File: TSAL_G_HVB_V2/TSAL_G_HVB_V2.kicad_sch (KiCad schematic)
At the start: 44 parts, among them J1 Conn_01x03_Pin, J2 Conn_01x02_Pin, J3 Conn_01x02_Pin, J4 Conn_01x02_Pin, Q1 2N7002, Q2 MMBT3904, Q3 PMOS, U1 uA7805, U2 74HC86, U3 74AHC04, U4 74LS09, U5 NE555D

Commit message: TSAL GREEN SYSTEM V2 READY TO FAB
SCH&PCB updated for both HVB V2 and ACCUM V2

PCB is 9 draw at work btw
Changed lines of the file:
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@@
+		)
+	)
+	(global_label "SCS_SIGN_IN"
+		(shape input)
+		(at 45.466 152.908 180)
+		(fields_autoplaced yes)
+		(effects
+			(font
+				(size 1.27 1.27)
+			)
+			(justify right)
+		)
+		(property "Intersheetrefs" "${INTERSHEET_REFS}"
+			(at 30.5065 152.908 0)
+			(hide yes)
+			(show_name no)
+			(do_not_autoplace no)
+			(effects
+				(font
+					(size 1.27 1.27)
+				)
+				(justify right)
+			)
 		)
 	)
@@
 	(global_label "RELAY_AUX_STATE"
 		(shape input)
+		(at 50.038 157.734 180)
+		(fields_autoplaced yes)
+		(effects
+			(font
+				(size 1.27 1.27)
+			)
+			(justify right)
+		)
+		(property "Intersheetrefs" "${INTERSHEET_REFS}"
+			(at 30.4824 157.734 0)
+			(hide yes)
+			(show_name no)
+			(do_not_autoplace no)
+			(effects
+				(font
+					(size 1.27 1.27)
+				)
+				(justify right)
+			)
+		)
+	)
+	(global_label "HV_SIGN_IN"
+		(shape input)
+		(at 44.45 148.336 180)
+		(fields_autoplaced yes)
+		(effects
+			(font
+				(size 1.27 1.27)
+			)
+			(justify right)
+		)
+		(property "Intersheetrefs" "${INTERSHEET_REFS}"
+			(at 30.7604 148.336 0)
+			(hide yes)
+			(show_name no)
+			(do_not_autoplace no)
+			(effects
+				(font
+					(size 1.27 1.27)
+				)
+				(justify right)
+			)
+		)
+	)
+	(global_label "RELAY_AUX_STATE"
+		(shape input)
 		(at 32.258 32.512 0)
 		(fields_autoplaced yes)
@@
 			(hide yes)
 			(show_name no)
+			(do_not_autoplace no)
+			(effects
+				(font
+					(size 1.27 1.27)
+				)
+				(justify right)
+			)
+		)
+	)
+	(global_label "RELAY_INTENDED_STATE"
+		(shape input)
+		(at 55.626 163.322 180)
+		(fields_autoplaced yes)
+		(effects
+			(font
+				(size 1.27 1.27)
+			)
+			(justify right)
+		)
+		(property "Intersheetrefs" "${INTERSHEET_REFS}"
+			(at 30.6276 163.322 0)
+			(hide yes)
+			(show_name no)

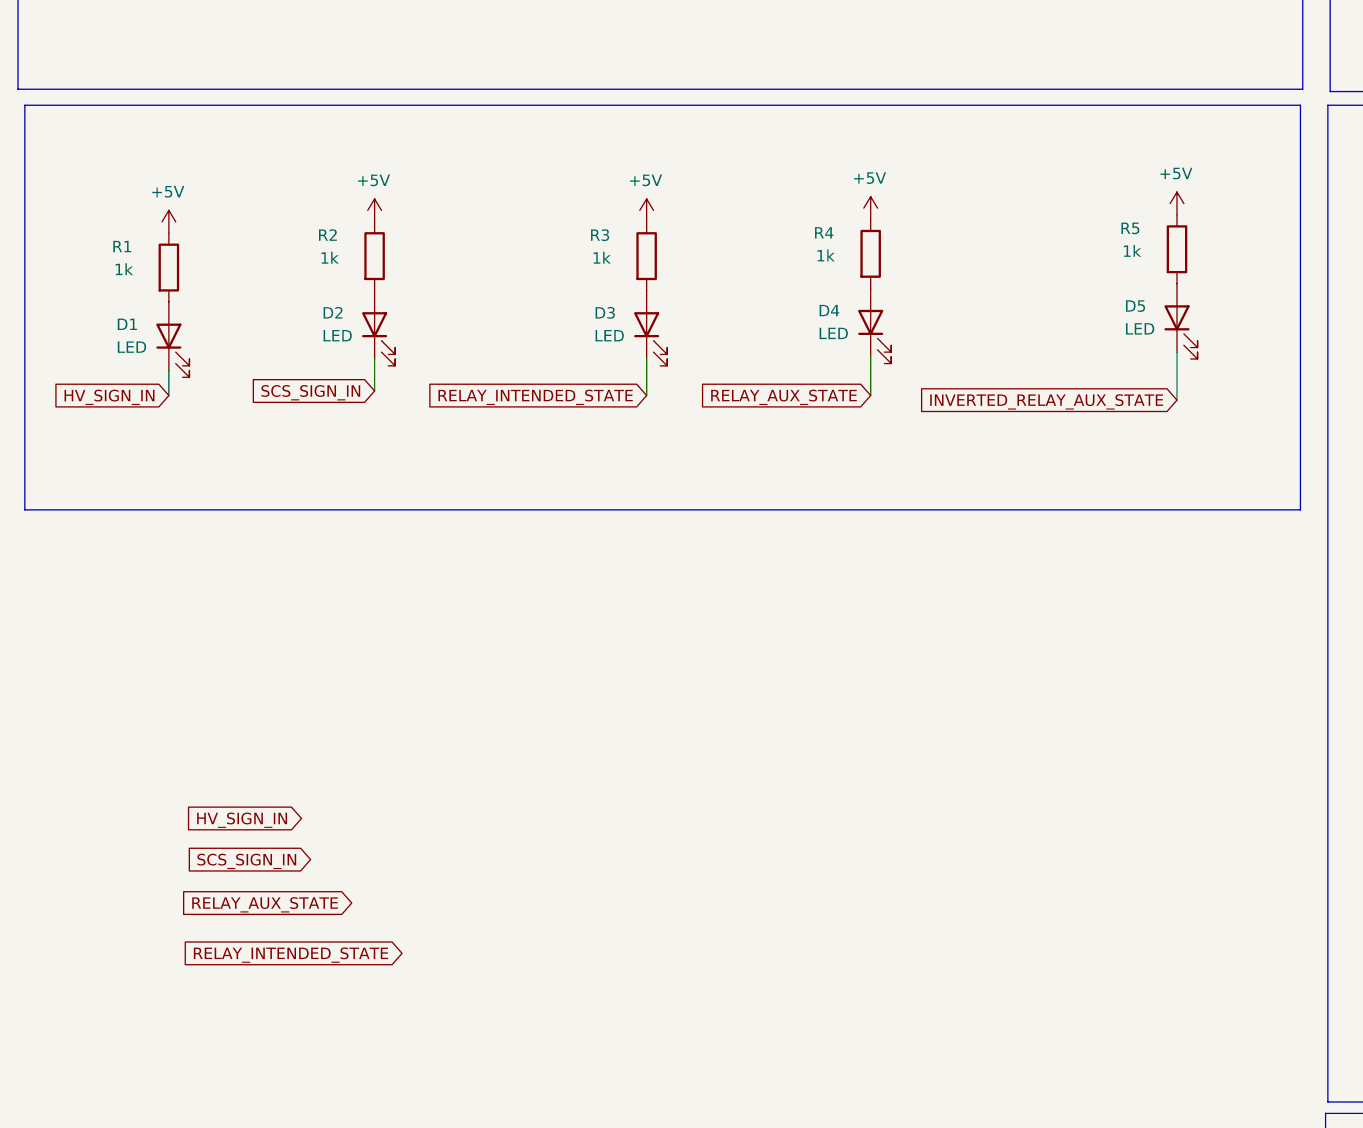
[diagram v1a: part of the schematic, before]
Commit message: ACCUM BOARDs BATCH ORDER
ts indicator
imd latch v2
tsalg accum v2.1
tsalg hvb v2.1
batch order
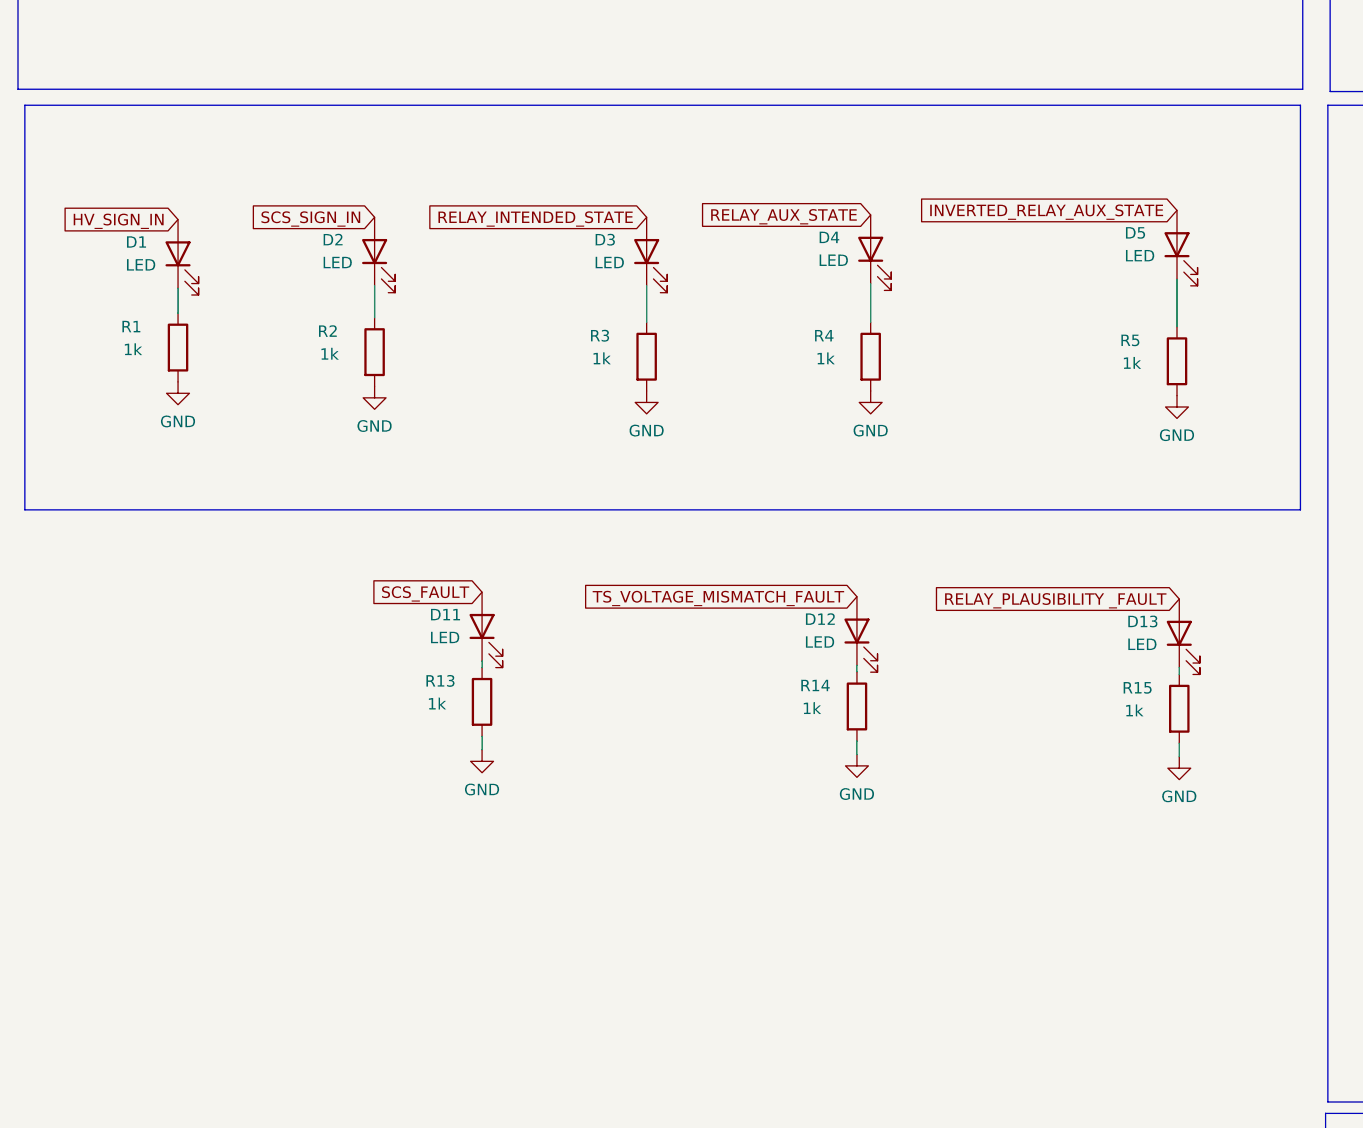
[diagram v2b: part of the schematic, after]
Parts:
- added D11, D12, D13: LED, RMC_LED:LED_0805_2012Metric_Pad1.45x1.40mm_HandSolder, symbol Device:LED
- added R13, R14, R15: 1k, RMC_Resistor:R_0805_2012Metric_Pad1.20x1.40mm_HandSolder_L, symbol Device:R
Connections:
- net +5V: no longer R1.1, R2.1, R3.1, R4.1, R5.1
- net GND: now also R1.2, R2.2, R3.2, R4.2, R5.2, R13.2, R14.2, R15.2
- net HV_SIGN_IN: now also D1.2 (A); no longer D1.1 (K)
- net INVERTED_RELAY_AUX_STATE: now also D5.2 (A); no longer D5.1 (K)
- net RELAY_AUX_STATE: now also D4.2 (A); no longer D4.1 (K)
- net RELAY_INTENDED_STATE: now also D3.2 (A); no longer D3.1 (K)
- net RELAY_PLAUSIBILITY _FAULT: now also D13.2 (A)
- net SCS_FAULT: now also D11.2 (A)
- net SCS_SIGN_IN: now also D2.2 (A); no longer D2.1 (K)
- net TS_VOLTAGE_MISMATCH_FAULT: now also D12.2 (A)
- new net: D3.1 (K), R3.1
- new net: D4.1 (K), R4.1
- new net: D12.1 (K), R14.1
- new net: D5.1 (K), R5.1
- new net: D13.1 (K), R15.1
- new net: D2.1 (K), R2.1
- new net: D11.1 (K), R13.1
- new net: D1.1 (K), R1.1
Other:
- moved on the sheet: D1, D2, D3, D4, D5, R1, R2, R3, R4, R5
